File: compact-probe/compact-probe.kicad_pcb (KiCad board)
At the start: 2 copper layers, 47.5 x 47.5 mm, 28 parts, among them IC1 ATA6561-GBQW-N, J1 Conn_01x08_Male, J2 Conn_01x04_Male, J3 Conn_02x05_Odd_Even, J4 Conn_01x01_Female, J5 Conn_01x01_Female, J6 Conn_01x01_Female, J7 Conn_01x01_Female, J8 Conn_01x01_Female, U4 ESP32-C3-WROOM-02-H4, U6 LT1963AxST-3.3

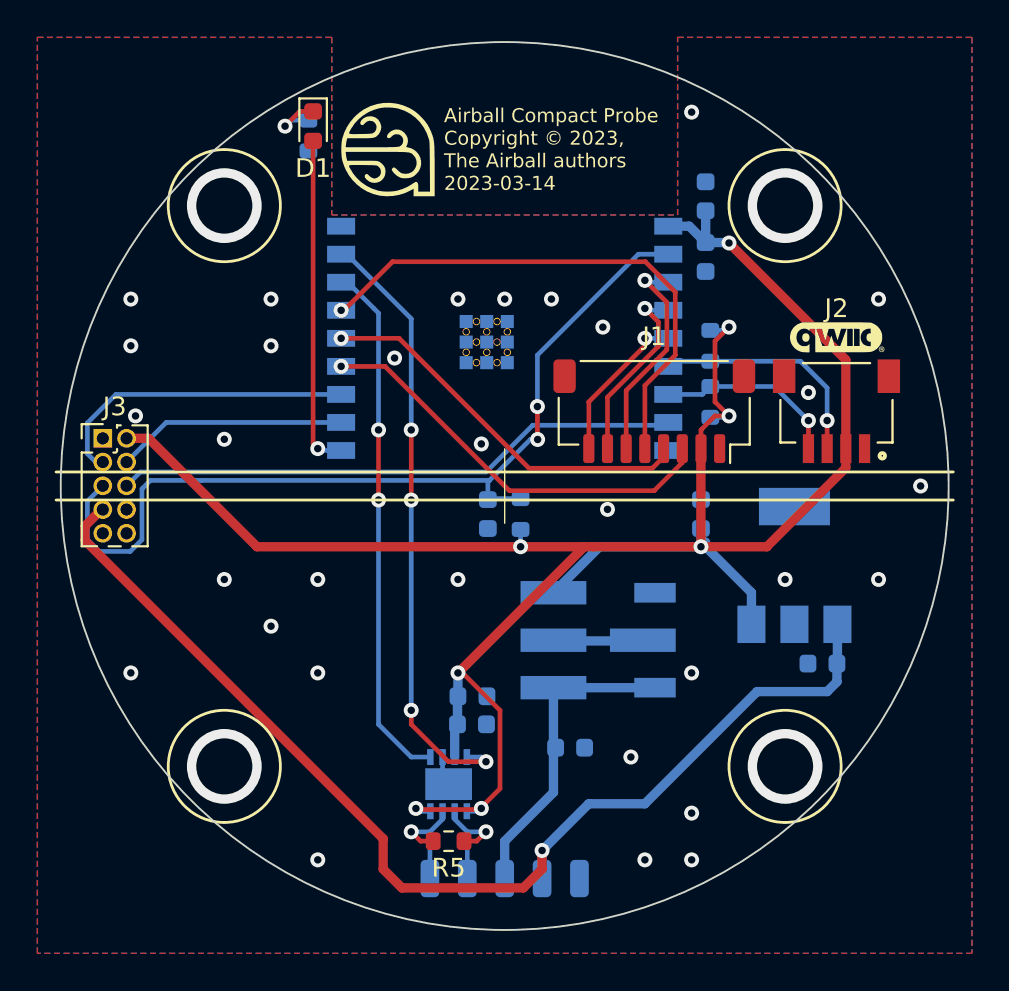
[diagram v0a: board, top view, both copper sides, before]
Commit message: Changed to new power supply and different CANBus chip.
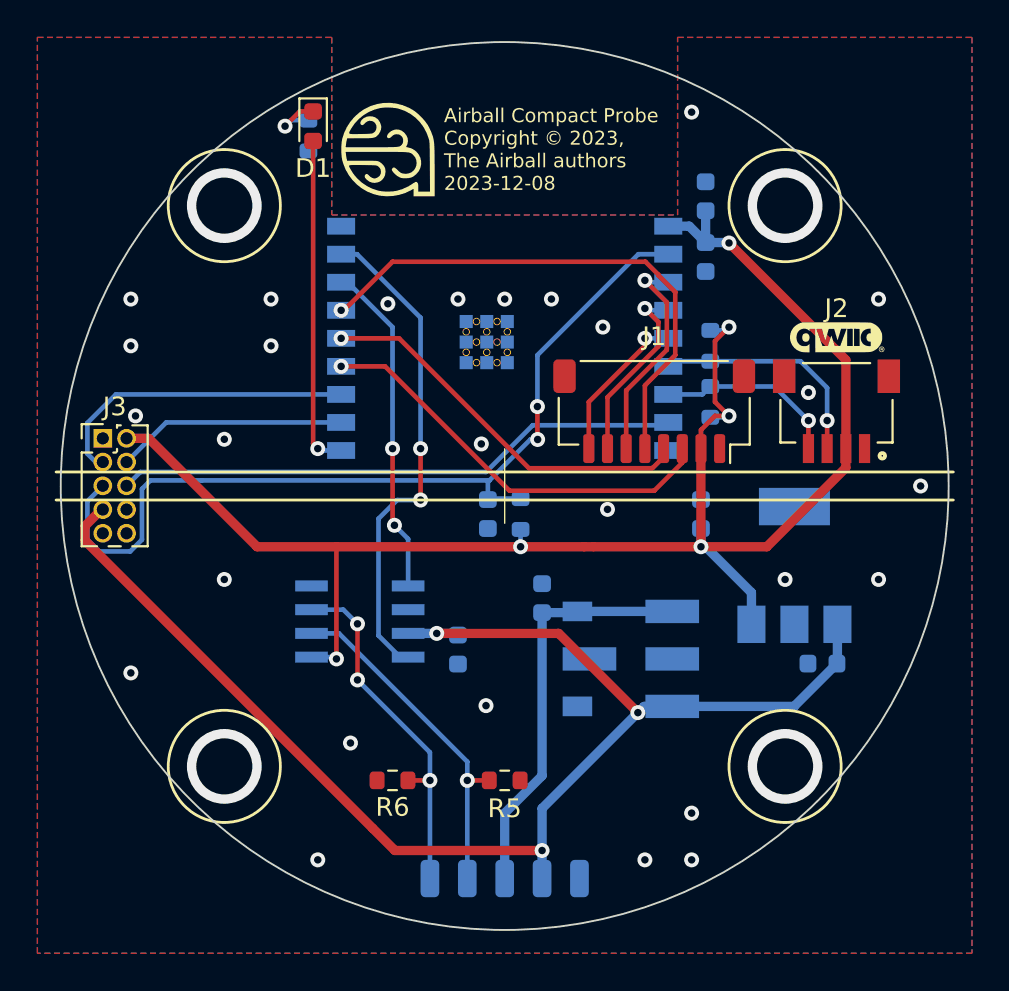
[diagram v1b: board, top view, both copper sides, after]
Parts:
- removed C10: 22uF, Capacitor_SMD:C_0603_1608Metric
- removed IC1: ATA6561-GBQW-N, airball-hardware:SON65P300X300X90-9N-D
- added R6: 60Ω, Resistor_SMD:R_0603_1608Metric, F.Cu at (-6.00, 15.8)
- added U1: TJA1051T_3_118, airball-hardware:TJA1051T_3_118, B.Cu at (-7.75, 7.25)
- C9: value 100nF -> 10uF
- PS1: value K7803MT-500R4 -> K7805MT-500R4; footprint airball-hardware:CONV_K7803MT-500R4 -> airball-hardware:CONV_K7805MT-500R4
- R5: value 120Ω -> 60Ω
- moved C1 8.14 mm to (2.00, 6.00), turned to 90 degrees
- moved R5 4.42 mm to (0.00, 15.8), turned to 0 degrees
- moved C9 4.07 mm to (-2.50, 8.75), turned to -90 degrees
- moved PS1 2.02 mm to (6.75, 9.25), turned to 180 degrees
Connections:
- C3 pad 1: VBAT -> VBAT_5V
- C9 pad 1: +3V3 -> VBAT_5V
- J3 pad 7: VBAT -> VBAT_5V
- J5 pad 1: VBAT -> VBAT_5V
- PS1 pad 3: +3V3 -> VBAT_5V
- R5 pad 2: CANH -> GND
- U6 pad 1: VBAT -> VBAT_5V
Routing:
- net VBAT_5V: track 0.00 -> 73.5 mm, vias 0 -> 3
- net VBAT: track 60.7 -> 0.00 mm, vias 1 -> 0
- net +3V3: track 122.3 -> 92.5 mm, vias 8 -> 6
- net CANH: track 6.26 -> 19.2 mm, vias 1 -> 3
- net CANL: track 6.26 -> 18.6 mm
- net CAN_TX: track 28.3 -> 17.9 mm
- net GND: track 7.01 -> 0.00 mm, vias 35 -> 31
- net CAN_RX: track 32.8 -> 26.4 mm, vias 4 -> 2
- net 12V28: track 16.7 -> 22.0 mm
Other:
- board text added: "Airball Compact Probe Copyright © 2023, The Airball authors 2023-12-08"
- board text added: "VBAT_5V"
- board text removed: "Airball Compact Probe Copyright © 2023, The Airball authors 2023-03-14"
- board text removed: "VBAT"
